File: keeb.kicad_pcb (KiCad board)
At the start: 2 copper layers, 134 parts, among them SW101 SW_Push, SW102 SW_Push, SW103 SW_Push, SW104 SW_Push, SW105 SW_Push, SW106 SW_Push, SW107 SW_Push, SW108 SW_Push, SW109 SW_Push, SW110 SW_Push, SW111 SW_Push, SW112 SW_Push, SW113 SW_Push, SW114 SW_Push, SW115 SW_Push, SW116 SW_Push, SW117 SW_Push, SW118 SW_Push, SW119 SW_Push, SW120 SW_Push, SW121 SW_Push, SW122 SW_Push, SW123 SW_Push, SW124 SW_Push, SW125 SW_Push, SW126 SW_Push, SW127 SW_Push, SW128 SW_Push, SW129 SW_Push, SW130 SW_Push, SW131 SW_Push, SW132 SW_Push, SW133 SW_Push, SW134 SW_Push, SW135 SW_Push, SW136 SW_Push, SW137 SW_Push, SW138 SW_Push, SW139 SW_Push, SW140 SW_Push, SW141 SW_Push, SW142 SW_Push, SW143 SW_Push, SW144 SW_Push, SW145 SW_Push, SW146 SW_Push, SW147 SW_Push, SW148 SW_Push, SW149 SW_Push, SW150 SW_Push, SW151 SW_Push, SW152 SW_Push, SW153 SW_Push, SW154 SW_Push, SW155 SW_Push, SW156 SW_Push, SW157 SW_Push, SW158 SW_Push, SW159 SW_Push, SW160 SW_Push, SW161 SW_Push, SW162 SW_Push, SW163 SW_Push, SW164 SW_Push, SW165 SW_Push, SW166 SW_Push

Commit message: init
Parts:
- moved SW156 291.0 mm to (334.0, 177.8)
- moved SW166 286.2 mm to (334.0, 196.8)
- moved SW154 273.7 mm to (295.9, 177.8)
- moved SW164 268.6 mm to (295.9, 196.8)
- moved SW162 242.8 mm to (238.8, 196.8)
- moved SW163 236.0 mm to (276.9, 196.8)
- moved H102 226.3 mm to (238.8, 196.8), turned to 180 degrees
- moved SW155 226.2 mm to (315.0, 177.8)
- moved SW165 223.2 mm to (315.0, 196.8)
- moved SW153 219.1 mm to (276.9, 177.8)
- moved SW141 209.2 mm to (315.0, 158.8)
- moved SW151 206.4 mm to (238.8, 177.8)
- moved SW142 197.8 mm to (334.0, 158.8)
- moved SW115 195.2 mm to (86.4, 139.7)
- moved SW161 187.1 mm to (181.6, 196.8)
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
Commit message: schem compl, layout sw, mat  routing
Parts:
- added C101: 100n, Capacitor_SMD:C_0603_1608Metric_Pad1.08x0.95mm_HandSolder, F.Cu at (206.4, 193.8)
- added C102: 100n, Capacitor_SMD:C_0603_1608Metric_Pad1.08x0.95mm_HandSolder, F.Cu at (207.0, 198.8)
- added C103: 100n, Capacitor_SMD:C_0603_1608Metric_Pad1.08x0.95mm_HandSolder, F.Cu at (208.3, 193.8)
- added C104: 100n, Capacitor_SMD:C_0603_1608Metric_Pad1.08x0.95mm_HandSolder, F.Cu at (214.0, 198.8)
- added C105: 100n, Capacitor_SMD:C_0603_1608Metric_Pad1.08x0.95mm_HandSolder, F.Cu at (213.4, 193.8)
- added C106: 20p, Capacitor_SMD:C_0603_1608Metric_Pad1.08x0.95mm_HandSolder, B.Cu at (224.8, 203.2)
- added C107: 20p, Capacitor_SMD:C_0603_1608Metric_Pad1.08x0.95mm_HandSolder, B.Cu at (224.8, 189.2)
- added C108: 1u, Capacitor_SMD:C_0603_1608Metric_Pad1.08x0.95mm_HandSolder, F.Cu at (210.2, 193.8)
- added F101: 500mA, Fuse:Fuse_1206_3216Metric_Pad1.42x1.75mm_HandSolder, B.Cu at (199.2, 107.7)
- added J101: USB_C_Receptacle_USB2.0, Connector_USB:USB_C_Receptacle_Palconn_UTC16-G, F.Cu at (208.2, 107.2)
- added R101: 5K1, Resistor_SMD:R_0603_1608Metric_Pad0.98x0.95mm_HandSolder, F.Cu at (190.9, 103.5)
- added R102: 5K1, Resistor_SMD:R_0603_1608Metric_Pad0.98x0.95mm_HandSolder, F.Cu at (190.8, 105.5)
- added R103: 22, Resistor_SMD:R_0603_1608Metric_Pad0.98x0.95mm_HandSolder, B.Cu at (209.0, 187.5)
- added R104: 22, Resistor_SMD:R_0603_1608Metric_Pad0.98x0.95mm_HandSolder, B.Cu at (207.3, 187.5)
- added R105: 10k, Resistor_SMD:R_0603_1608Metric_Pad0.98x0.95mm_HandSolder, F.Cu at (190.6, 107.3)
- added R106: 10k, Resistor_SMD:R_0603_1608Metric_Pad0.98x0.95mm_HandSolder, B.Cu at (205.1, 203.2)
- added SW167: SW_Push, Button_Switch_THT:SW_PUSH_6mm_H5mm, F.Cu at (216.9, 104.5)
- added U101: TPD2EUSB30, Package_TO_SOT_SMD:Texas_DRT-3, B.Cu at (208.2, 112.3)
- added U102: ATmega32U4-AU, Package_QFP:TQFP-44_10x10mm_P0.8mm, B.Cu at (210.2, 196.2)
- added Y101: 16MHZ/20PF, Crystal:Crystal_HC49-4H_Vertical, B.Cu at (224.8, 198.8)
- moved D166 275.7 mm to (342.9, 199.4)
- moved D165 261.6 mm to (323.9, 199.4)
- moved D164 232.6 mm to (304.8, 199.4)
- moved D156 219.5 mm to (342.9, 180.3)
- moved D163 218.9 mm to (285.8, 199.4)
- moved D115 205.8 mm to (95.2, 142.2)
- moved D117 200.3 mm to (133.3, 142.2)
- moved D154 191.5 mm to (304.8, 180.3)
- moved D102 188.6 mm to (114.3, 123.2)
- moved D157 186.3 mm to (95.2, 199.4)
- moved D129 182.5 mm to (95.2, 161.3)
- moved D155 179.1 mm to (323.9, 180.3)
- moved D116 179.1 mm to (114.3, 142.2)
- moved D162 174.5 mm to (247.7, 199.4)
- moved D153 170.3 mm to (285.8, 180.3)
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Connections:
- D113 pad 1: Net-(D113-Pad1) -> ROW_0
- D114 pad 1: Net-(D113-Pad1) -> ROW_0
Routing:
- net ROW_0: track 0.00 -> 322.9 mm, vias 0 -> 1
- net ROW_1: track 0.00 -> 305.0 mm, vias 0 -> 1
- net ROW_2: track 0.00 -> 287.1 mm, vias 0 -> 1
- net ROW_3: track 0.00 -> 270.1 mm, vias 0 -> 1
- net ROW_4: track 0.00 -> 254.9 mm, vias 0 -> 1
- net COL_0: track 0.00 -> 91.4 mm
- net COL_11: track 0.00 -> 90.1 mm
- net COL_5: track 0.00 -> 90.1 mm
- net COL_13: track 0.00 -> 90.1 mm
- net COL_10: track 0.00 -> 90.1 mm
- net COL_2: track 0.00 -> 90.1 mm
- net COL_1: track 0.00 -> 90.1 mm
- net COL_8: track 0.00 -> 90.1 mm
- net COL_3: track 0.00 -> 90.1 mm
- net COL_12: track 0.00 -> 90.1 mm
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- added copper zone on B.Cu, net GND
- added copper zone on F.Cu, net GND

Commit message: col, USB, and gnd layout
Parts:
- removed U101: TPD2EUSB30, Package_TO_SOT_SMD:Texas_DRT-3
- added J102: AVR-ISP-6, Connector_PinHeader_2.54mm:PinHeader_2x03_P2.54mm_Vertical, F.Cu at (219.6, 217.9)
- F101: moved to F.Cu
- J101, R101, R102, R105: moved to B.Cu
- moved SW167 110.8 mm to (207.0, 214.9)
- moved R105 109.4 mm to (202.6, 216.1), turned to 270 degrees
- moved R102 25.3 mm to (211.6, 119.9), turned to 270 degrees
- moved R101 23.5 mm to (207.8, 119.9), turned to 270 degrees
- moved F101 12.7 mm to (210.3, 113.8)
- moved C102 8.11 mm to (213.6, 194.1), turned to 270 degrees
- moved J101 7.55 mm to (209.7, 114.6), turned to 0 degrees
- moved C104 6.83 mm to (207.3, 199.9), turned to 0 degrees
- moved C105 6.09 mm to (212.9, 199.9), turned to 180 degrees
- moved C101 2.51 mm to (208.9, 194.1)
- moved C103 1.79 mm to (206.5, 194.1)
- moved R103 1.52 mm to (209.0, 185.9)
- moved R104 1.52 mm to (207.3, 185.9)
- moved C108 1.08 mm to (211.2, 194.1)
- moved D112 0.51 mm to (304.3, 123.2)
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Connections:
- U102 pad 1: Net-(U102-Pad1) -> COL_6
- U102 pad 18: COL_6 -> SCL
- U102 pad 19: COL_7 -> SDA
- U102 pad 8: Net-(U102-Pad8) -> COL_7
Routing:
- net COL_0: track 91.4 -> 234.2 mm
- net COL_13: track 90.1 -> 217.4 mm
- net COL_1: track 90.1 -> 212.6 mm
- net COL_12: track 90.1 -> 197.0 mm
- net COL_2: track 90.1 -> 192.2 mm
- net COL_4: track 67.5 -> 155.0 mm
- net COL_11: track 90.1 -> 172.8 mm, vias 0 -> 1
- net COL_3: track 90.1 -> 170.3 mm, vias 0 -> 1
- net +5V: track 15.5 -> 92.0 mm, vias 5 -> 6
- net COL_10: track 90.1 -> 160.4 mm
- net COL_9: track 67.5 -> 126.3 mm
- net COL_5: track 90.1 -> 132.4 mm
- net COL_8: track 90.1 -> 111.0 mm
- net COL_7: track 67.5 -> 87.8 mm
- net COL_6: track 67.5 -> 86.6 mm
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- added copper zone on B.Cu, net +5V
- added copper zone on B.Cu, net D+
- added copper zone on B.Cu, net D-
- added copper zone on B.Cu, net VBUS
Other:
- board outline added: 266.7 x 98.7 mm

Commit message: models3D
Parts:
- removed Y101: 16MHZ/20PF, Crystal:Crystal_HC49-4H_Vertical
- added J1: AudioJack3, Connector_Audio:Jack_3.5mm_CUI_SJ-3523-SMT_Horizontal, B.Cu at (335.8, 203.1)
- added Y1: 16Mhz, Crystal:Crystal_SMD_2016-4Pin_2.0x1.6mm, B.Cu at (219.2, 195.3)
- C106, C107: value 20p -> 22p
- moved C106 7.41 mm to (221.0, 196.8), turned to 45 degrees
- moved C107 6.12 mm to (220.7, 193.8), turned to 315 degrees
- renumbered SW101 to SWe
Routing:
- net SCL: track 0.00 -> 128.1 mm, vias 0 -> 2
- net SDA: track 0.00 -> 127.2 mm, vias 0 -> 2
- net XTAL1: track 16.5 -> 5.12 mm, vias 1 -> 0
- net XTAL2: track 16.4 -> 5.55 mm, vias 1 -> 0
- net GND: track 1.90 -> 5.51 mm, vias 230 -> 231
- net COL_9: track 126.3 -> 128.9 mm
- net VBUS: track 8.84 -> 10.3 mm
- net COL_8: track 111.0 -> 112.0 mm
- net ROW_4: track 254.9 -> 255.0 mm, vias 1 -> 3

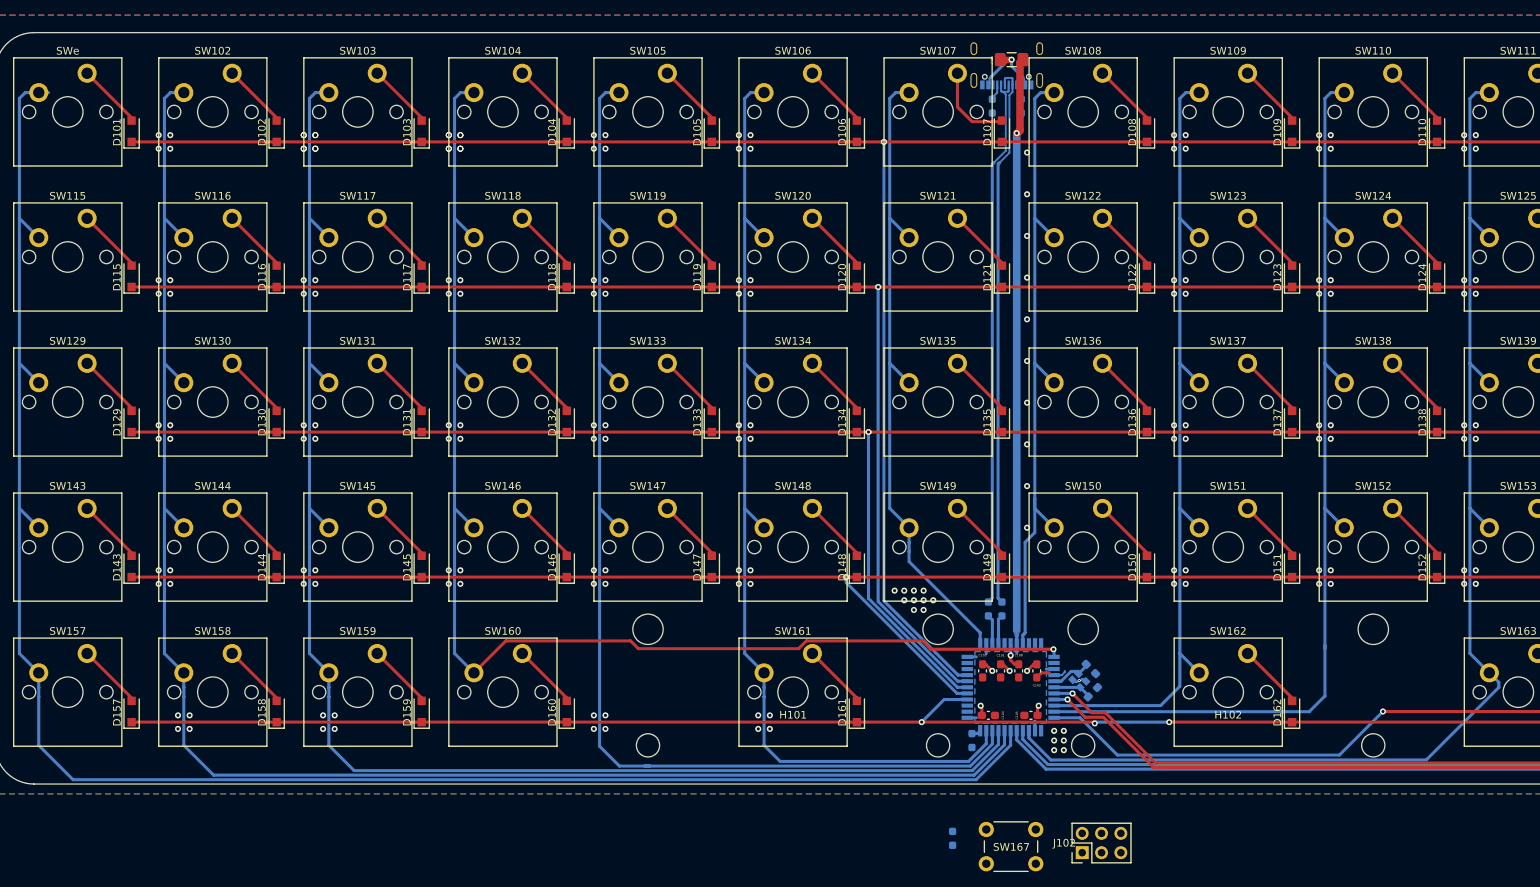
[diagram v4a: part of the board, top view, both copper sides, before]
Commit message: first pass layout complete
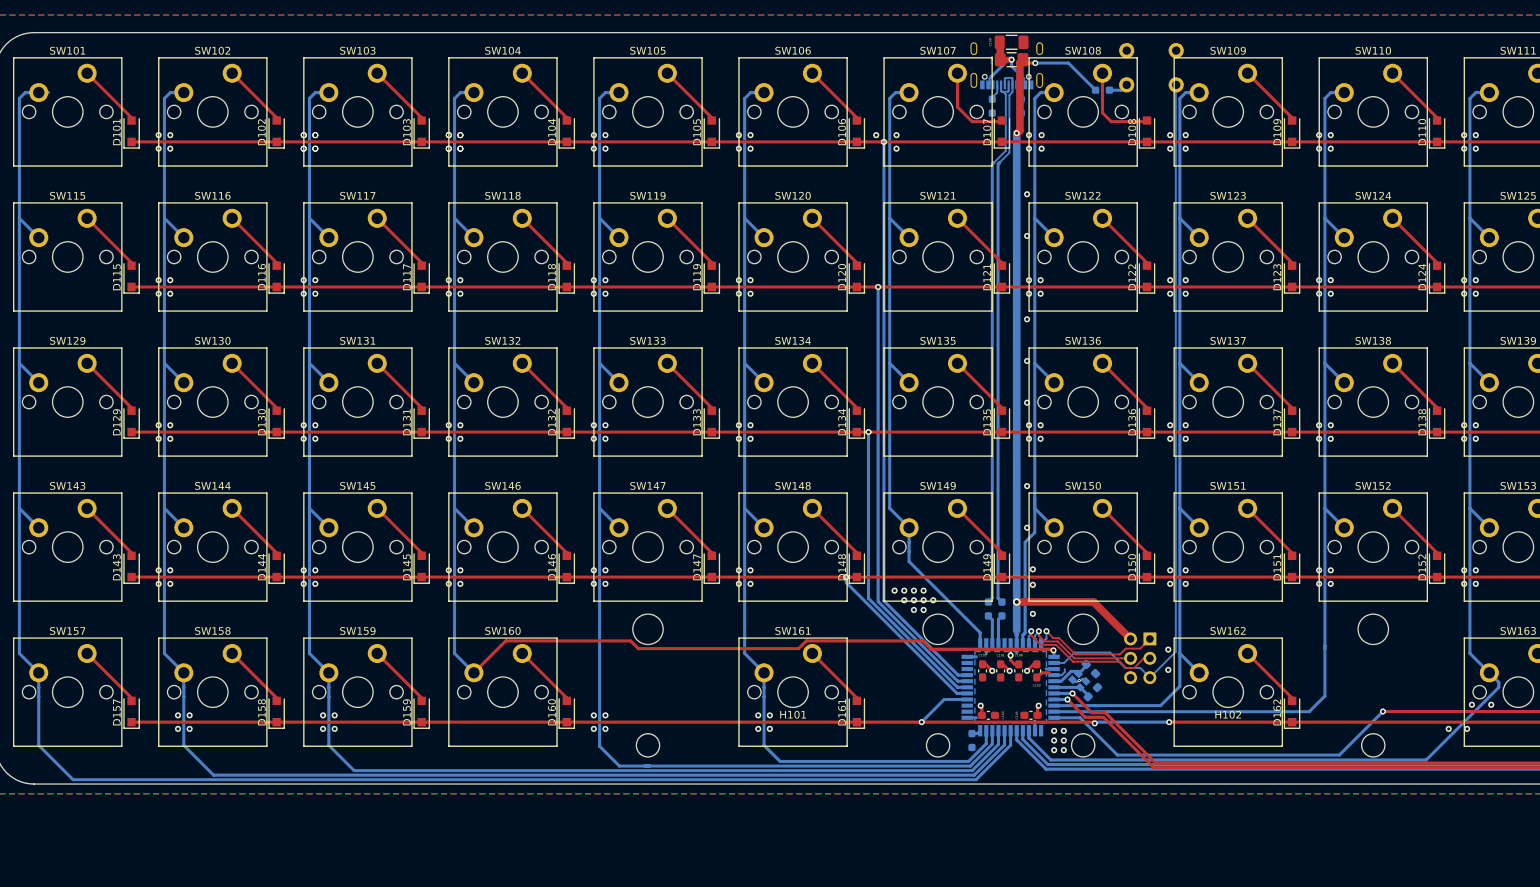
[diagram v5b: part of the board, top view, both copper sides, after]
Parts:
- removed SW167: SW_Push, Button_Switch_THT:SW_PUSH_6mm_H5mm
- added C109: 10u, Capacitor_SMD:C_1206_3216Metric_Pad1.33x1.80mm_HandSolder, F.Cu at (210.3, 111.5)
- added RESET: SW_Push, Button_Switch_THT:SW_PUSH_6mm_H5mm, B.Cu at (225.4, 117.1)
- J102: moved to B.Cu
- moved R105 100.2 mm to (222.2, 117.8), turned to 180 degrees
- moved J102 29.4 mm to (228.5, 189.9), turned to 180 degrees
- renumbered SWe to SW101
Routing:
- net ~RESET: track 0.00 -> 96.2 mm
- net +5V: track 92.0 -> 120.1 mm, vias 6 -> 8
- net SCLK: track 0.00 -> 20.2 mm, vias 0 -> 1
- net MISO: track 0.00 -> 17.6 mm, vias 0 -> 1
- net MOSI: track 0.00 -> 15.7 mm, vias 0 -> 1
- net Net-(D108-Pad2): track 8.77 -> 11.6 mm
- net VBUS: track 10.3 -> 12.6 mm
- net GND: track 5.51 -> 5.75 mm, vias 231 -> 252

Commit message: lp rst sw
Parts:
- RESET: footprint Button_Switch_THT:SW_PUSH_6mm_H5mm -> Button_Switch_SMD:SW_SPST_B3U-1000P
- moved R105 5.04 mm to (226.6, 115.2), turned to 90 degrees
- moved RESET 4.15 mm to (229.1, 115.2), turned to 90 degrees
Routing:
- net +5V: track 120.1 -> 123.9 mm
- net ~RESET: track 96.2 -> 99.4 mm
